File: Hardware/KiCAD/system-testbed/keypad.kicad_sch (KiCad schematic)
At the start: 43 parts, among them J1 HW-834 Module, SW1 1, SW10 6, SW11 9, SW12 #, SW13 UP, SW14 DOWN, SW15 LEFT, SW16 RIGHT, SW17 PTT, SW18 MENU, SW19 EXIT, SW2 4, SW20 SK0, SW3 7, SW4 *, SW5 2, SW6 5, SW7 8, SW8 0, SW9 3

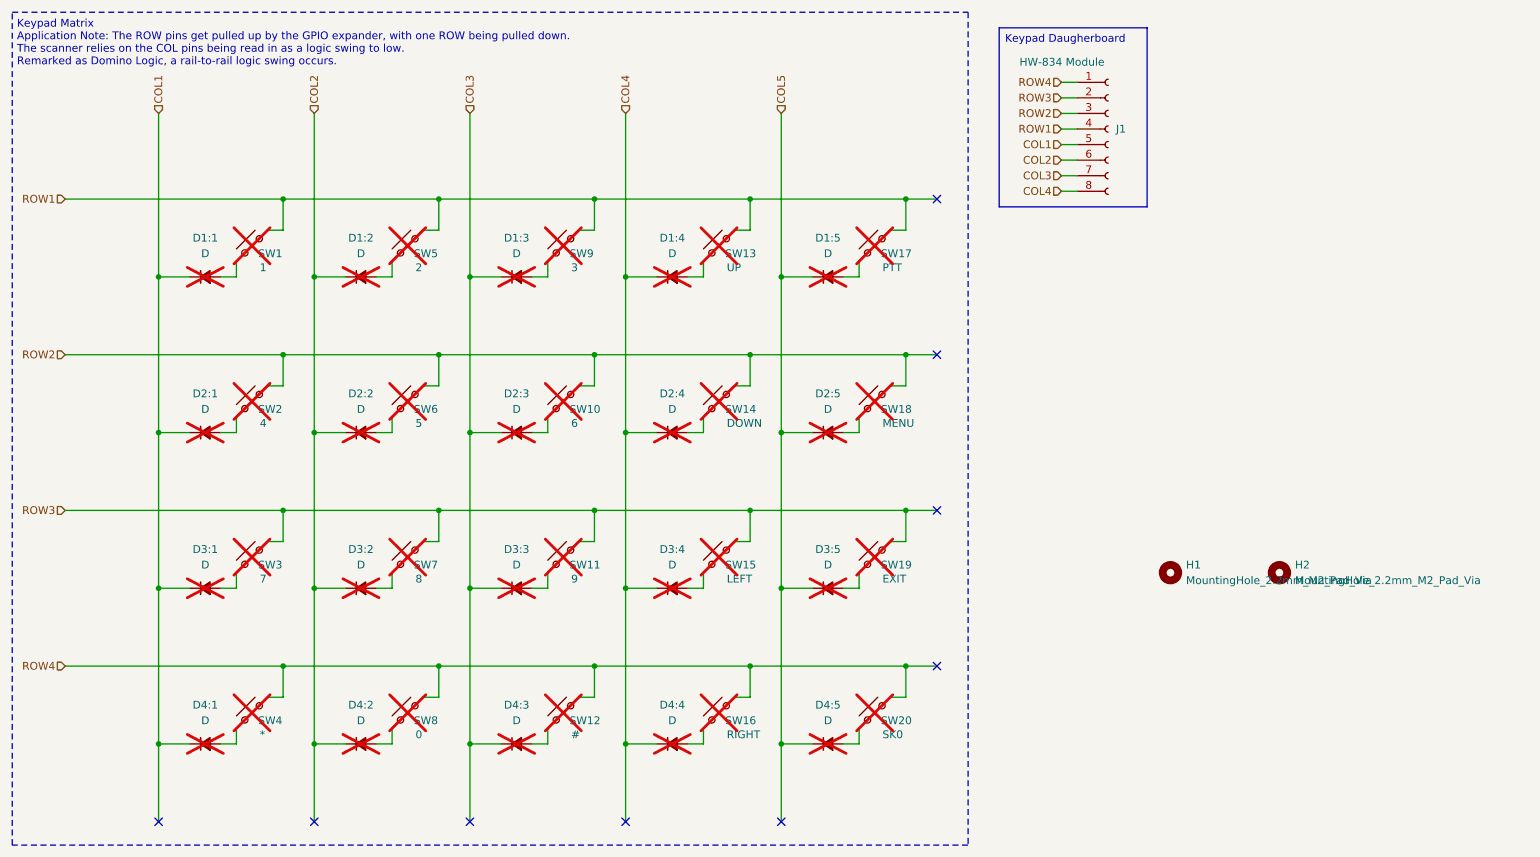
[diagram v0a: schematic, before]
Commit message: fix: move port expander over to HMI schematic #15 #33
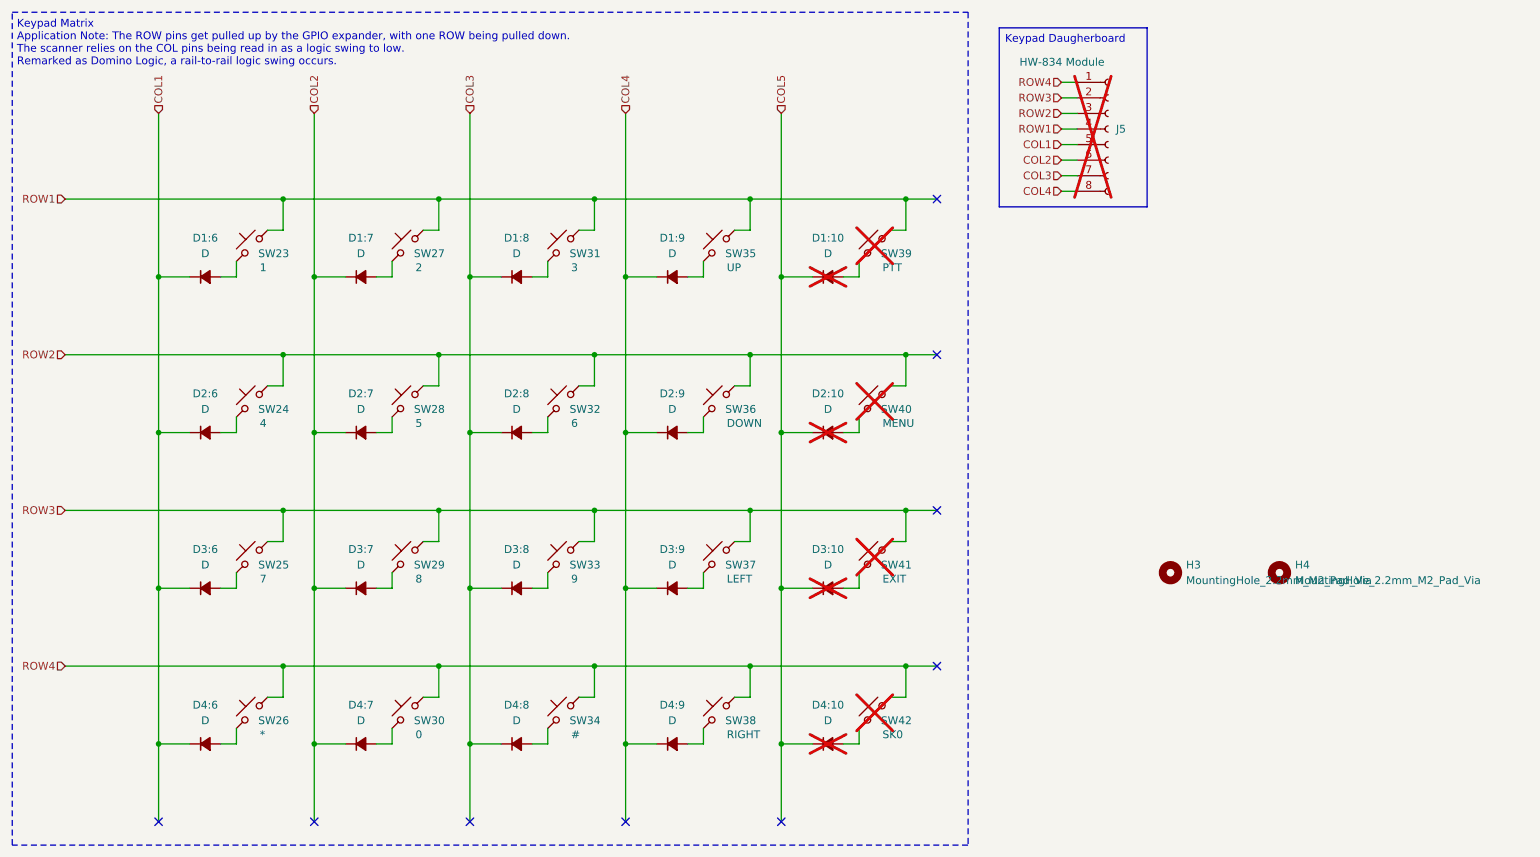
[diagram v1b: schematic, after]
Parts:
- D1:6: renamed from D1:1; now fitted; now in the parts list
- D1:7: renamed from D1:2; now fitted; now in the parts list
- D1:8: renamed from D1:3; now fitted; now in the parts list
- D1:9: renamed from D1:4; now fitted; now in the parts list
- D2:6: renamed from D2:1; now fitted; now in the parts list
- D2:7: renamed from D2:2; now fitted; now in the parts list
- D2:8: renamed from D2:3; now fitted; now in the parts list
- D2:9: renamed from D2:4; now fitted; now in the parts list
- D3:6: renamed from D3:1; now fitted; now in the parts list
- D3:7: renamed from D3:2; now fitted; now in the parts list
- D3:8: renamed from D3:3; now fitted; now in the parts list
- D3:9: renamed from D3:4; now fitted; now in the parts list
- D4:6: renamed from D4:1; now fitted; now in the parts list
- D4:7: renamed from D4:2; now fitted; now in the parts list
- D4:8: renamed from D4:3; now fitted; now in the parts list
- D4:9: renamed from D4:4; now fitted; now in the parts list
- J5: renamed from J1; now not fitted; now left out of the parts list
- SW23: renamed from SW1; now fitted; now in the parts list
- SW24: renamed from SW2; now fitted; now in the parts list
- SW25: renamed from SW3; now fitted; now in the parts list
- SW26: renamed from SW4; now fitted; now in the parts list
- SW27: renamed from SW5; now fitted; now in the parts list
- SW28: renamed from SW6; now fitted; now in the parts list
- SW29: renamed from SW7; now fitted; now in the parts list
- SW30: renamed from SW8; now fitted; now in the parts list
- SW31: renamed from SW9; now fitted; now in the parts list
- SW32: renamed from SW10; now fitted; now in the parts list
- SW33: renamed from SW11; now fitted; now in the parts list
- SW34: renamed from SW12; now fitted; now in the parts list
- SW35: renamed from SW13; now fitted; now in the parts list
- SW36: renamed from SW14; now fitted; now in the parts list
- SW37: renamed from SW15; now fitted; now in the parts list
- SW38: renamed from SW16; now fitted; now in the parts list
- renumbered D1:5 to D1:10, D2:5 to D2:10, D3:5 to D3:10, D4:5 to D4:10, H1 to H3, H2 to H4, SW17 to SW39, SW18 to SW40, SW19 to SW41, SW20 to SW42

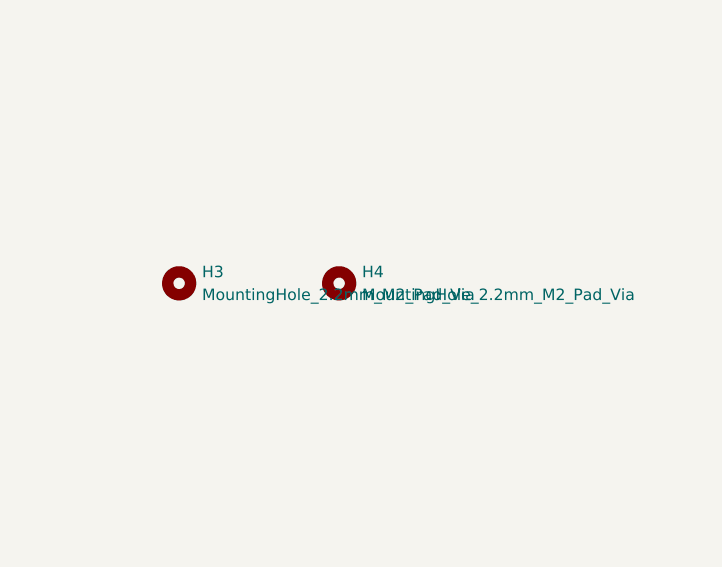
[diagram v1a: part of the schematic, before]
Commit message: fix: remove mounting holes for unused HW-834 keypad #69
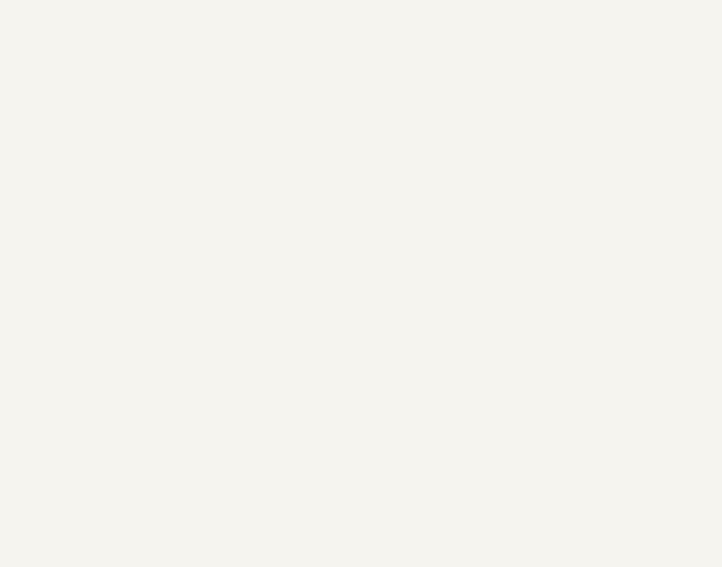
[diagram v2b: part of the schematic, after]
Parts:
- removed H3: MountingHole_2.2mm_M2_Pad_Via, MountingHole:MountingHole_2.2mm_M2_Pad_Via, symbol Mechanical:MountingHole
- removed H4: MountingHole_2.2mm_M2_Pad_Via, MountingHole:MountingHole_6.4mm_M6_Pad_Via, symbol Mechanical:MountingHole
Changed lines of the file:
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@@
-	)
-	(symbol
-		(lib_id "Mechanical:MountingHole")
-		(at 220.98 105.41 0)
-		(unit 1)
-		(exclude_from_sim yes)
-		(in_bom no)
-		(on_board yes)
-		(dnp no)
-		(fields_autoplaced yes)
-		(property "Reference" "H4"
-			(at 223.52 104.1399 0)
-			(effects
-				(font
-					(size 1.27 1.27)
-				)
-				(justify left)
-			)
-		)
-		(property "Value" "MountingHole_2.2mm_M2_Pad_Via"
-			(at 223.52 106.6799 0)
-			(effects
-				(font
-					(size 1.27 1.27)
-				)
-				(justify left)
-			)
-		)
-		(property "Footprint" "MountingHole:MountingHole_6.4mm_M6_Pad_Via"
-			(at 220.98 105.41 0)
-			(effects
-				(font
-					(size 1.27 1.27)
-				)
-				(hide yes)
-			)
-		)
-		(property "Datasheet" "~"
-			(at 220.98 105.41 0)
-			(effects
-				(font
-					(size 1.27 1.27)
-				)
-				(hide yes)
-			)
-		)
-		(property "Description" ""
-			(at 220.98 105.41 0)
-			(effects
-				(font
-					(size 1.27 1.27)
-				)
-				(hide yes)
-			)
-		)
-		(instances
-			(project "system-testbed"
-				(path "/72756aea-0ff9-4757-9699-8d0f18588f6f/8dcdcb54-0a4a-4913-bd90-1e0f545b8046/7aad1b45-8286-4cab-8d27-66dd29006c0b"
-					(reference "H4")
-					(unit 1)
-				)
-			)
-		)
 	)
 	(symbol
@@
 					(unit 1)
 				)
-			)
-		)
-	)
-	(symbol
-		(lib_id "Mechanical:MountingHole")
-		(at 203.2 105.41 0)
-		(unit 1)
-		(exclude_from_sim yes)
-		(in_bom no)
-		(on_board yes)
-		(dnp no)
-		(fields_autoplaced yes)
-		(property "Reference" "H3"
-			(at 205.74 104.1399 0)
-			(effects
-				(font
-					(size 1.27 1.27)
-				)
-				(justify left)
-			)
-		)
-		(property "Value" "MountingHole_2.2mm_M2_Pad_Via"
-			(at 205.74 106.6799 0)
-			(effects
-				(font
-					(size 1.27 1.27)
-				)
-				(justify left)
-			)
-		)
-		(property "Footprint" "MountingHole:MountingHole_2.2mm_M2_Pad_Via"
-			(at 203.2 105.41 0)
-			(effects
-				(font
-					(size 1.27 1.27)
-				)
-				(hide yes)
-			)
-		)
-		(property "Datasheet" "~"
-			(at 203.2 105.41 0)
-			(effects
-				(font
-					(size 1.27 1.27)
-				)
-				(hide yes)
-			)
-		)
-		(property "Description" ""
-			(at 203.2 105.41 0)
-			(effects
-				(font
-					(size 1.27 1.27)
-				)
-				(hide yes)
-			)
-		)
-		(instances
-			(project "system-testbed"
-				(path "/72756aea-0ff9-4757-9699-8d0f18588f6f/8dcdcb54-0a4a-4913-bd90-1e0f545b8046/7aad1b45-8286-4cab-8d27-66dd29006c0b"
-					(reference "H3")
-					(unit 1)
-				)
